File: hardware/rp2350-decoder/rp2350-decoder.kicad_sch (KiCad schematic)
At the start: 68 parts, among them J1 SWDIO, J2 SWCLK, J3 5052702412, Q1 DMN2991UDA-7B, Q2 DMN2991UDA-7B, Q3 NST847BPDP6T5G, Q4 NST847BPDP6T5G, Q5 DMN2991UDA-7B, Q6 DMN2991UDA-7B, Q7 DMN2991UDA-7B, Q8 DMN2991UDA-7B, SW1 BOOT, U1 NCS2220AMUT1G, U2 AP63203WU, U3 W25Q128JVPIQ, U4 RP2350A, U5 MAX98357AEWL+T, U6 MD9927, Y1 ABM8-272-T3

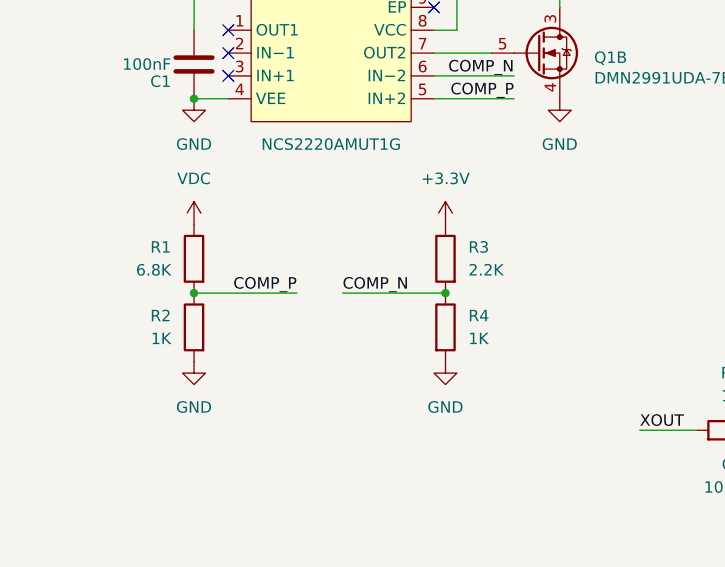
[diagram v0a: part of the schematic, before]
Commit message: fix: un-swap capacitor shutdown circuit inputs
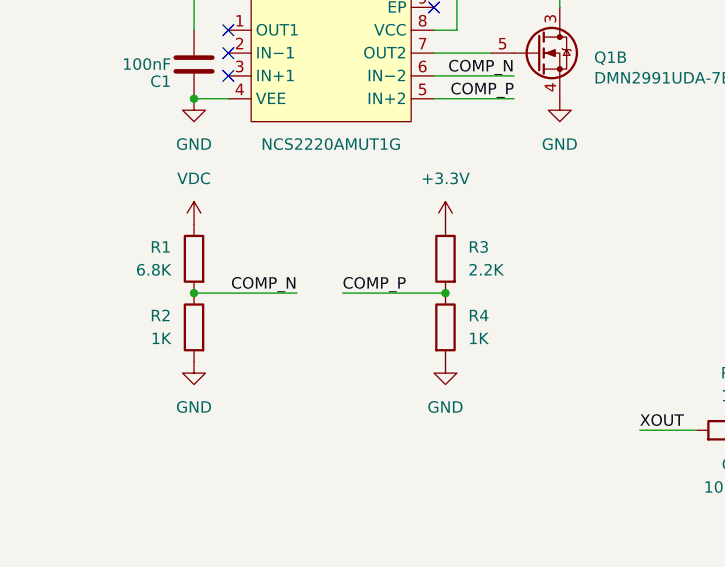
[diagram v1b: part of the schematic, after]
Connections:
- net COMP_N: now also R1.2, R2.1; no longer R3.2, R4.1
- net COMP_P: now also R3.2, R4.1; no longer R1.2, R2.1
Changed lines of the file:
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@@
 	)
 	(label "COMP_N"
-		(at 53.34 152.4 0)
-		(effects
-			(font
-				(size 1.27 1.27)
-			)
-			(justify left bottom)
+		(at 48.26 152.4 180)
+		(effects
+			(font
+				(size 1.27 1.27)
+			)
+			(justify right bottom)
 		)
 	)
@@
 	)
 	(label "COMP_P"
-		(at 48.26 152.4 180)
-		(effects
-			(font
-				(size 1.27 1.27)
-			)
-			(justify right bottom)
-		)
-	)
+		(at 53.34 152.4 0)
+		(effects
+			(font
+				(size 1.27 1.27)
+			)
+			(justify left bottom)
+		)
+	)

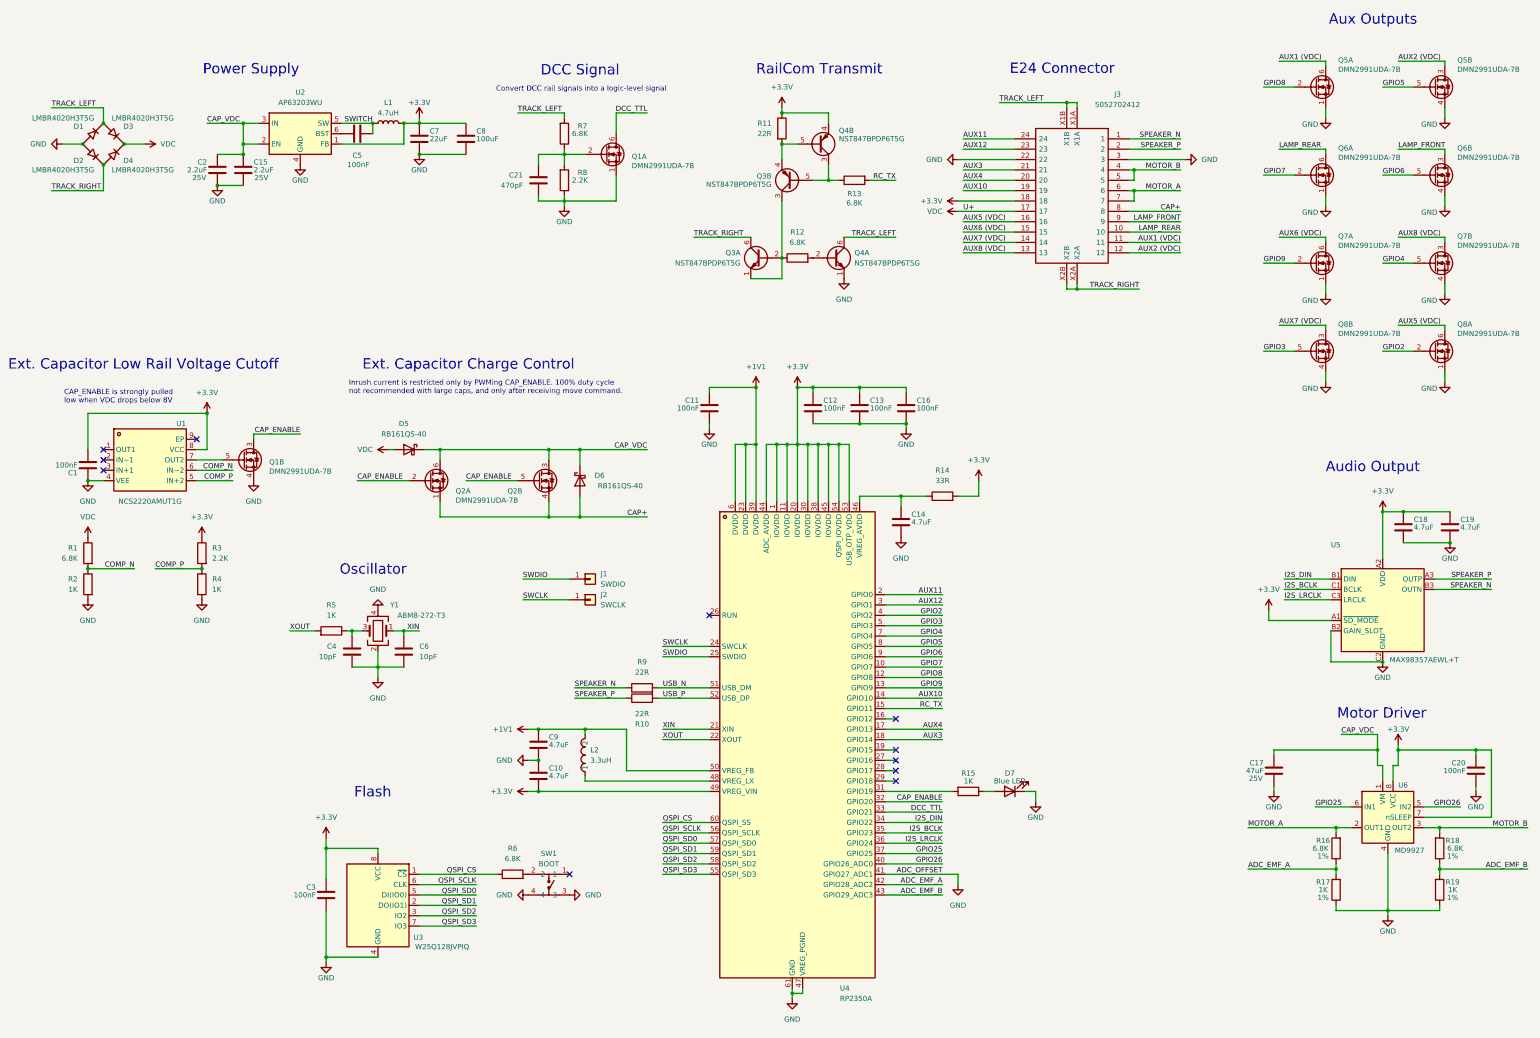
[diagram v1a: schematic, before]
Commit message: feat: zener diodes to detect both waves and cutouts
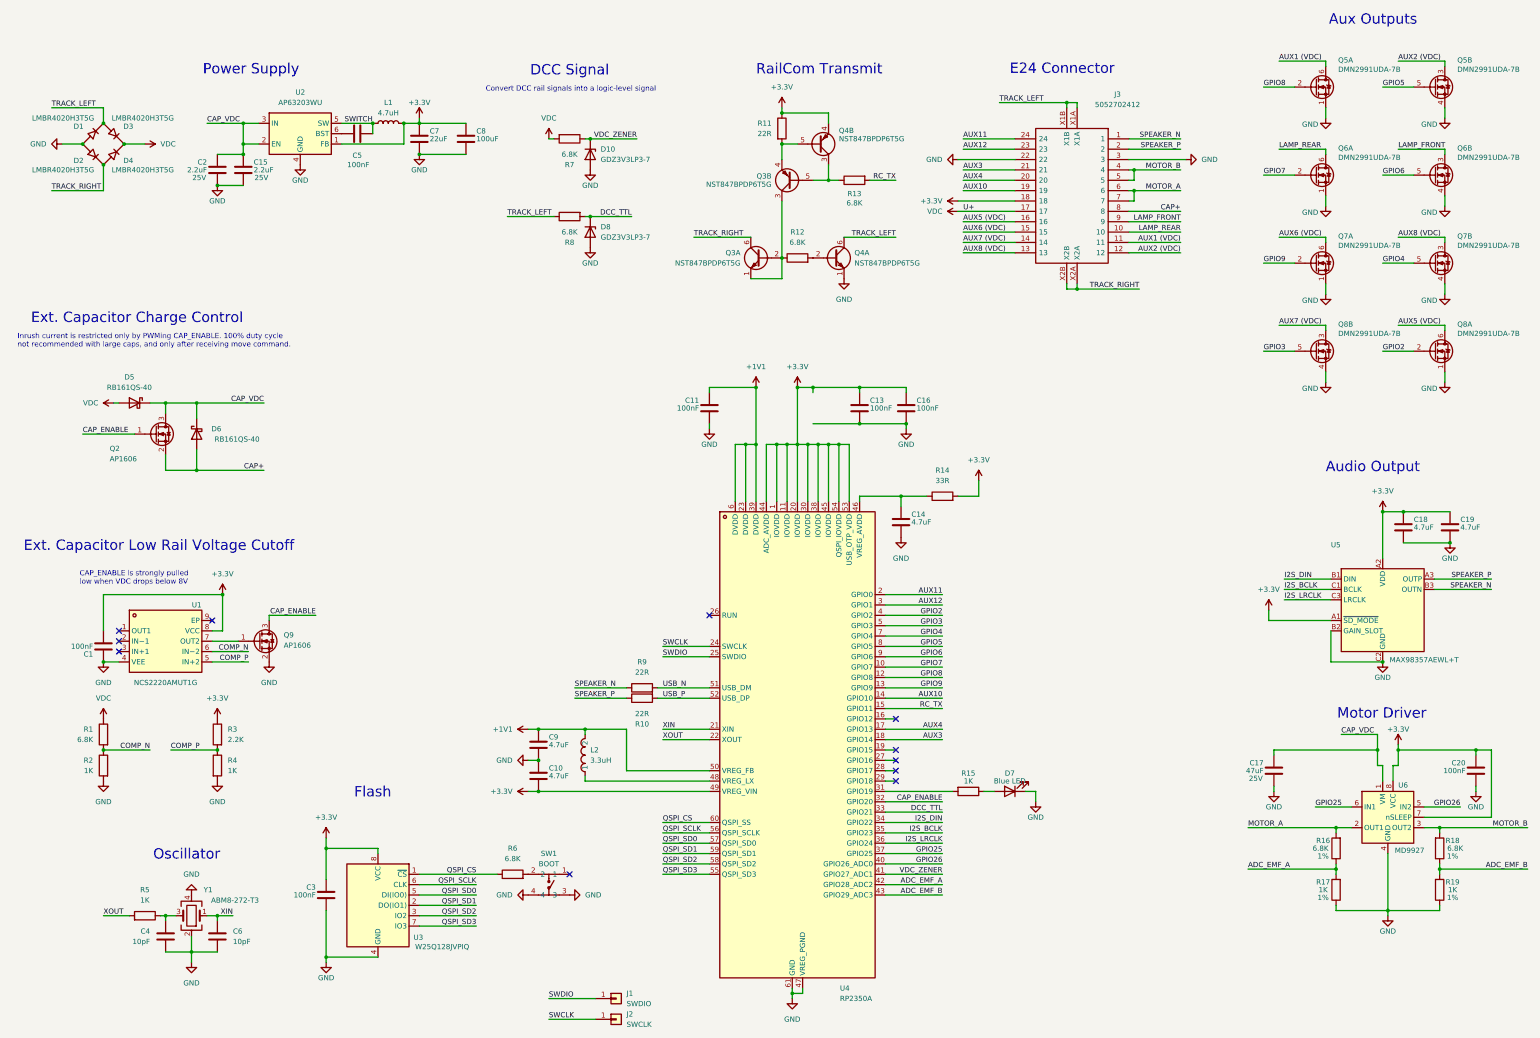
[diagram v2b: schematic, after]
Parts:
- removed C12: 100nF, rp2350-decoder:C_0201_0603Metric, symbol rp2350-decoder:C
- removed C21: 470pF, rp2350-decoder:C_0201_0603Metric, symbol rp2350-decoder:C
- removed Q1, Q2: DMN2991UDA-7B, rp2350-decoder:X2-DFN0806-6_L0.8-W0.6_X2-DFN0806-6, symbol rp2350-decoder:DMN2991UDA-7B
- added D10, D8: GDZ3V3LP3-7, rp2350-decoder:D_0201_0603Metric, symbol rp2350-decoder:D_Zener
- added Q2, Q9: AP1606, rp2350-decoder:Diodes_DFN1006-3, symbol rp2350-decoder:Q_NMOS_GSD
- R8: value 2.2K -> 6.8K; LCSC C473534 -> C423451; Tolerance 10% -> (none)
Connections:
- net CAP+: now also Q2.2 (S)
- net CAP_ENABLE: now also Q2.1 (G), Q9.3 (D)
- net CAP_VDC: now also Q2.3 (D)
- net DCC_TTL: now also R8.2, D8.1 (K)
- net GND: now also D10.2 (A), D8.2 (A), Q9.2 (S); no longer R8.1, U4.41 (GPIO27_ADC1)
- net TRACK_LEFT: now also R8.1; no longer R7.2
- net VDC: now also R7.2
- net VDC_ZENER: now reaches R7.1
- net VDC_ZENER: now also U4.41 (GPIO27_ADC1), D10.1 (K); no longer R8.2
- net at U1.7 (OUT2): now also Q9.1 (G)
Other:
- moved on the sheet: C1, C4, C6, D5, D6, J1, J2, R1, R2, R3, R4, R5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
